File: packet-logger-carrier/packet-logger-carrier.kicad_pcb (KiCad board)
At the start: 2 copper layers, 86 x 58 mm, 22 parts, among them J1 RAK19003 J6, J10 RAK SPARE, J11 ESP SPARE, J12 BATT IN, J13 BATT JST-PH, J14 BATT TO RAK, J15 J15, J2 RAK19003 J7, J3 XIAO ESP32-C6, J4 microSD, J5 LID CABLE, SW1 USER BUTTON, SW2 POWER SWITCH

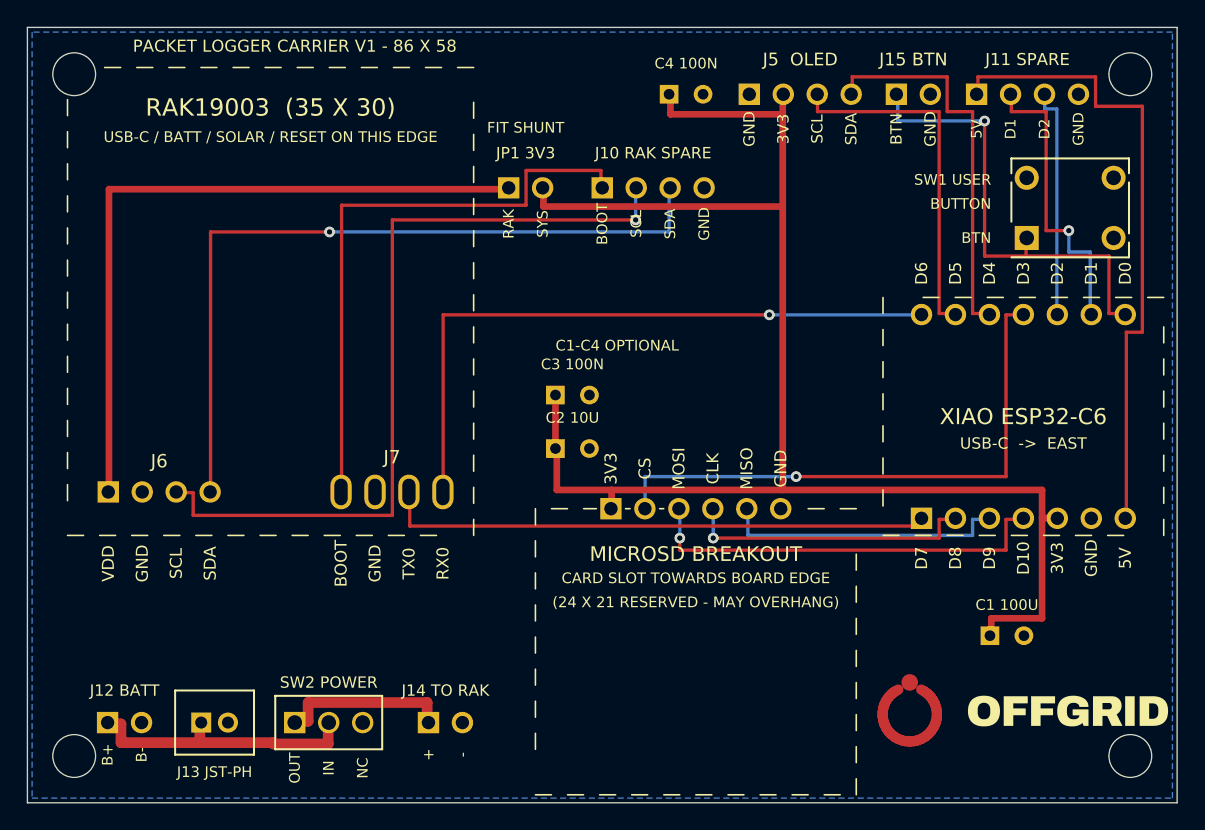
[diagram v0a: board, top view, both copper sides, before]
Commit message: hardware: add teardrops and make the router prefer roomy paths
Two more rounds of the same concern - traces sitting close to pads, and joints
meeting pads at what looked like an angle. Both now addressed properly.

TEARDROPS (src/teardrops.py)
Flares the trace where it meets a pad, built from real track segments on the
same net so KiCad connectivity and our DRC treat them as ordinary copper. This
removes the acute trace/pad corner entirely and puts metal at the joint.

Three bugs found while building it, each caught by a check rather than by eye:

  - the flare ran straight on past where the trace turned, landing on whatever
    was next door: 41 clearance violations. Now clamped to its own segment.
  - the span was measured from the track endpoint rather than the pad centre,
    which are not the same point, so one flare overshot: 1 dangling end.
  - a flare was generated from a segment that merely PASSED NEAR a pad rather
    than terminating in it, leaving copper floating beside the trace. Now
    requires the segment to run through the pad centre (perp <= 0.08 mm).

Also splits the underlying trace at each flare tip so the tip meets a real
vertex - without that KiCad reported 14 dangling ends.

ROOMIER ROUTING
The router now pays a cost for cells within 0.22 mm of foreign copper: still
legal, just discouraged, so traces drift to the middle of a gap instead of
hugging one edge. Free - same 8 vias, one extra segment.

Measured on the pads that prompted this:

    pad 13 (D1)   0.397 -> 0.597 mm
    pad 14 (D0)   0.355 -> 0.555 mm

Board-wide clearance distribution, before -> after:
    0.30-0.40 mm    74 -> 2
    0.40-0.60 mm     8 -> 58
    0.60 mm plus   188 -> 517

Worth recording for the record: none of this was necessary for manufacture.
The tightest spot was already 2.4x the 0.127 mm fab minimum, and every one of
those traces runs under soldermask, so solder cannot bridge to them. It is a
better board, not a rescued one.

All gates pass. KiCad 10 DRC: 0 erro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
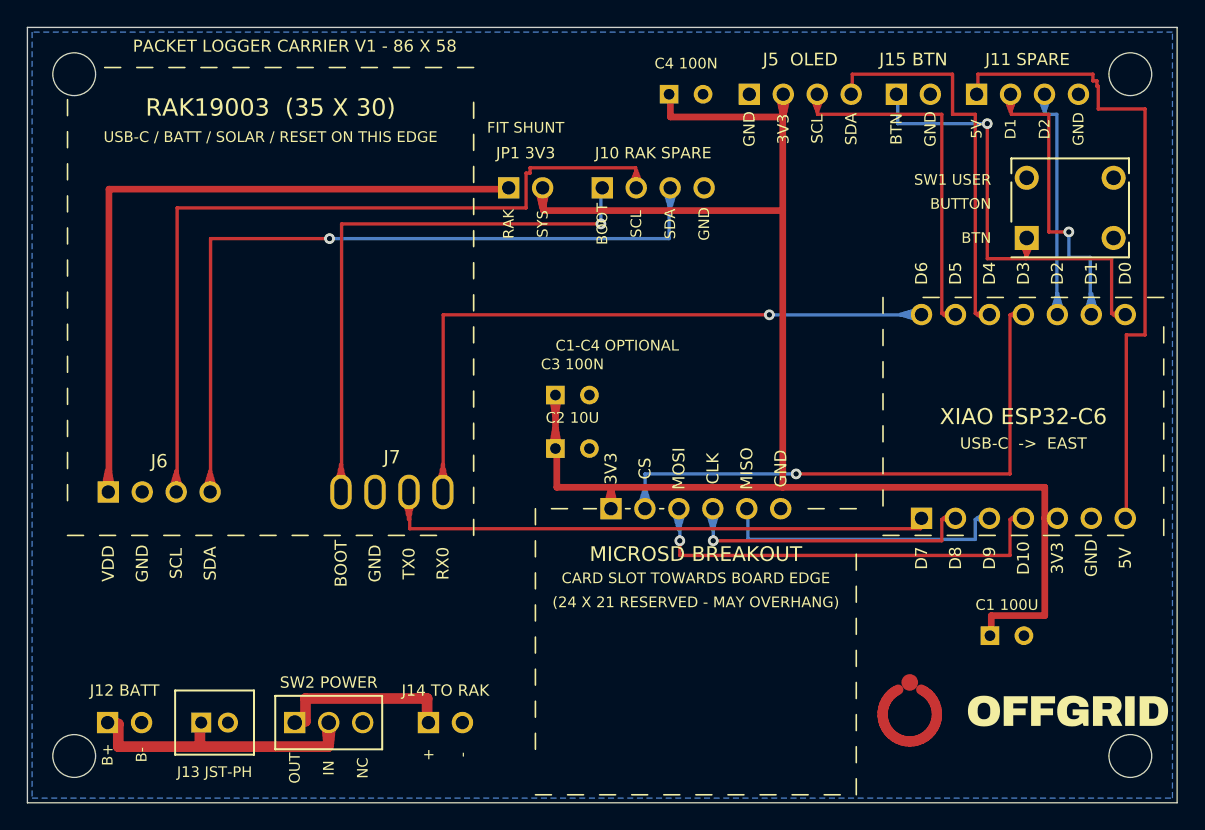
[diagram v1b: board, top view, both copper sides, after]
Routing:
- net +3V3: track 118.6 -> 127.4 mm
- net RAK_RX0: track 48.5 -> 52.1 mm
- net SD_MOSI: track 30.9 -> 34.1 mm
- net RAK_TX0: track 40.8 -> 43.9 mm
- net RAK_SDA: track 56.9 -> 60.0 mm
- net XIAO_D1: track 22.2 -> 25.0 mm
- net XIAO_D2: track 17.2 -> 20.0 mm
- net SD_CLK: track 21.6 -> 24.4 mm
- net SD_CS: track 42.6 -> 45.0 mm
- net BTN: track 34.6 -> 37.0 mm
- net RAK_SCL: track 60.4 -> 62.7 mm, vias 1 -> 0
- net BAT+: track 20.8 -> 23.0 mm
- net OLED_SCL: track 26.6 -> 28.7 mm
- net RAW_3V3: track 52.4 -> 53.9 mm
- net SD_MISO: track 21.1 -> 22.6 mm
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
